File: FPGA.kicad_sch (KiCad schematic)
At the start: 14 parts, among them U1 XC7A35T-CSG325

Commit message: FPGA Power
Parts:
- added C23, C31, C38, C45, C52: 47uF, symbol Device:C_Small
- added C24, C28, C29, C30, C34, C35, C36, C37, C41, C42, C43, C44, C48, C49, C50, C51: 470nF, symbol Device:C_Small
- added C25: 100uF, symbol Device:C_Small
- added C26, C27, C32, C33, C39, C40, C46, C47: 4.7uF, symbol Device:C_Small
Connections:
- net +1V0: now also U1.F7 (VCCINT), U1.F9 (VCCINT), U1.G8 (VCCINT), U1.H7 (VCCINT), U1.H9 (VCCINT), U1.J12 (VCCINT), U1.J8 (VCCINT), U1.K11 (VCCINT), U1.K7 (VCCINT), U1.L12 (VCCINT), U1.L8 (VCCINT), U1.M11 (VCCINT), U1.M7 (VCCINT), U1.N10 (VCCINT), U1.N12 (VCCINT), U1.N8 (VCCINT), U1.P11 (VCCINT), U1.P9 (VCCINT), C23.2, C24.2, C25.2, C26.2, C27.2, C28.2, C29.2, C30.2
- net +1V8: now also U1.E10 (VCCO_0), U1.R10 (VCCO_0), C52.2
- net GND: now also U1.J9 (GNDADC_0), C23.1, C24.1, C25.1, C26.1, C27.1, C28.1, C29.1, C30.1, C31.1, C32.1, C33.1, C34.1, C35.1, C36.1, C37.1, C38.1, C39.1, C40.1, C41.1, C42.1, C43.1, C44.1, C45.1, C46.1, C47.1, C48.1, C49.1, C50.1, C51.1, C52.1
- net +3V3: now reaches U1.L6 (VCCO_34)
- net +3V3: now also U1.M3 (VCCO_34), U1.P7 (VCCO_34), U1.R4 (VCCO_34), U1.T1 (VCCO_34), U1.V5 (VCCO_34), C45.2, C46.2, C47.2, C48.2, C49.2, C50.2, C51.2
- net +1V35: now reaches U1.A16 (VCCO_15)
- net +1V35: now also U1.B13 (VCCO_15), U1.C10 (VCCO_15), U1.D17 (VCCO_15), U1.E14 (VCCO_15), U1.G18 (VCCO_15), U1.H15 (VCCO_15), U1.L16 (VCCO_14), U1.P17 (VCCO_14), U1.R14 (VCCO_14), U1.T11 (VCCO_14), U1.U18 (VCCO_14), U1.U8 (VCCO_14), U1.V15 (VCCO_14), C31.2, C32.2, C33.2, C34.2, C35.2, C36.2, C37.2, C38.2, C39.2, C40.2, C41.2, C42.2, C43.2, C44.2

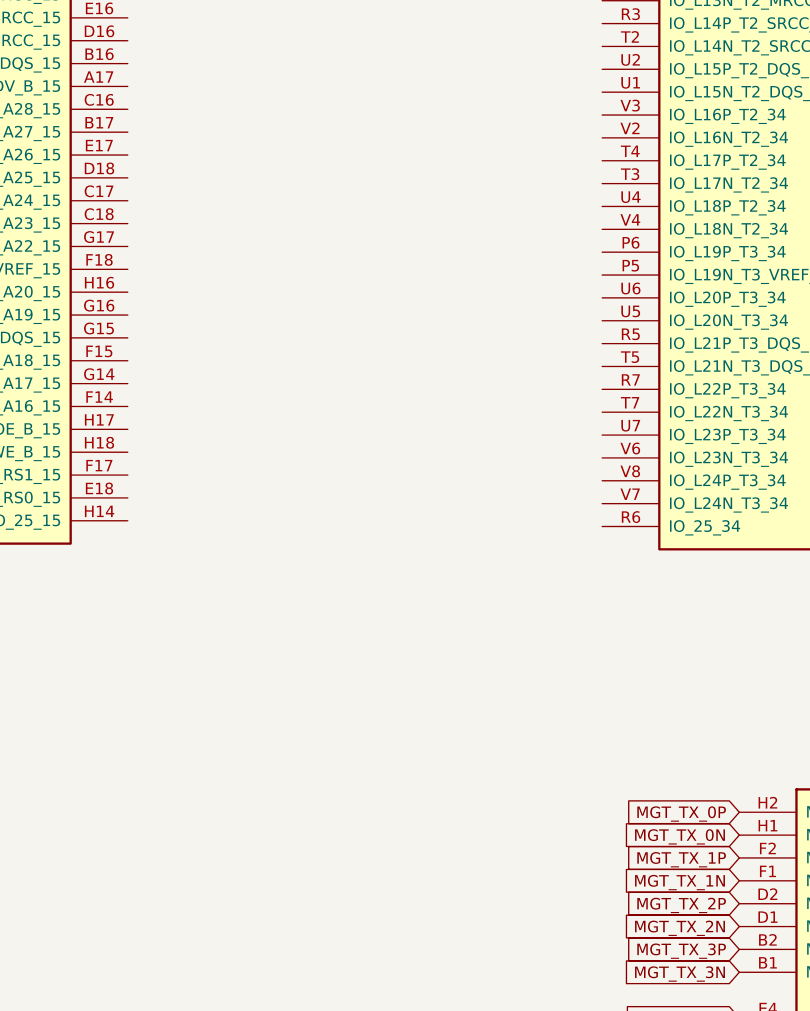
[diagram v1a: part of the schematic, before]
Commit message: DDR Labels
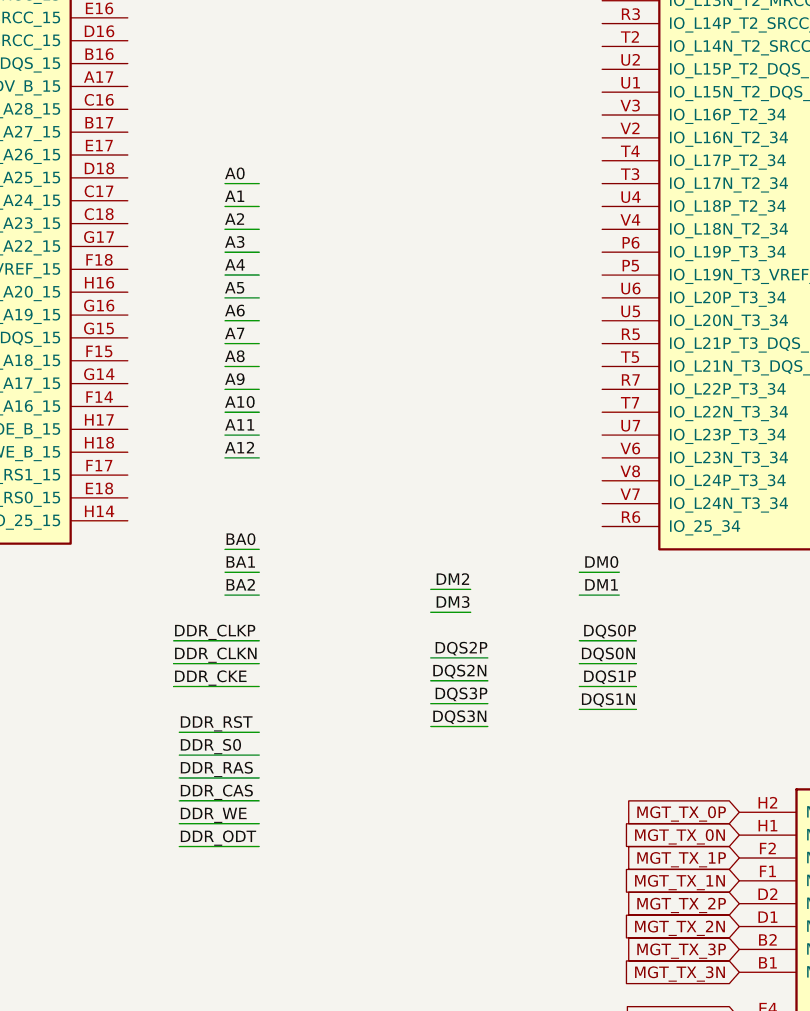
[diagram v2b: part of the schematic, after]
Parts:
- U1: footprint (none) -> Footprints:BGA324C80P18X18_1500X1500X150
